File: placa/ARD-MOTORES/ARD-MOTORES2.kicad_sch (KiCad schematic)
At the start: 24 parts, among them J1 Power, J2 Digital/PWM, J3 Analog, J4 Digital/PWM, J5 Conn_01x02, Q1 LFRZ44

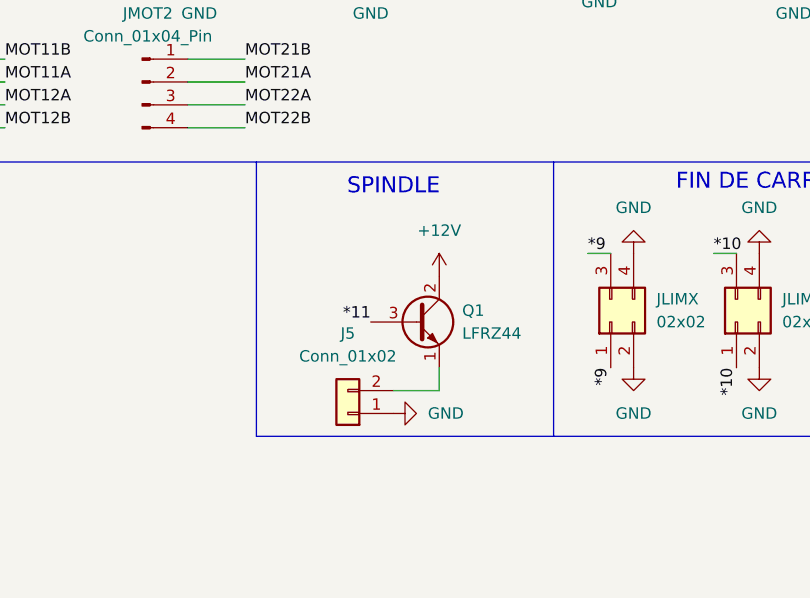
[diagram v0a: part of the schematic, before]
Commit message: arduino como main
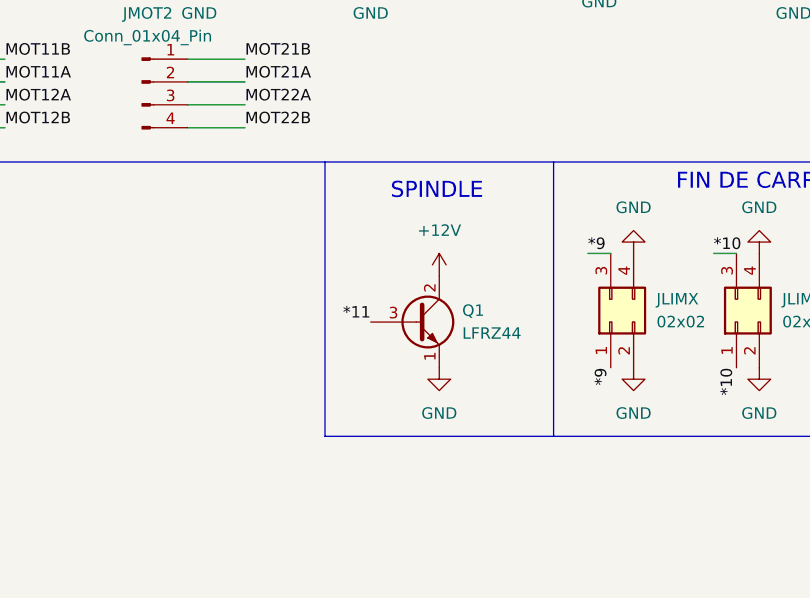
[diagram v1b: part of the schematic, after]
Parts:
- removed J5: Conn_01x02, symbol Connector_Generic:Conn_01x02
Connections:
- net GND: now also Q1.1 (E)
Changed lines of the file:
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@@
 	(polyline
 		(pts
-			(xy 204.47 115.57) (xy 204.47 85.09)
+			(xy 212.09 115.57) (xy 212.09 85.09)
 		)
 		(stroke
@@
 	(polyline
 		(pts
-			(xy 237.49 115.57) (xy 204.47 115.57)
+			(xy 237.49 115.57) (xy 212.09 115.57)
 		)
 		(stroke
@@
 	(wire
 		(pts
-			(xy 224.79 110.49) (xy 224.79 107.95)
-		)
-		(stroke
-			(width 0)
-			(type default)
-		)
-	)
-	(wire
-		(pts
 			(xy 135.89 43.18) (xy 139.7 43.18)
 		)
@@
 	(wire
 		(pts
-			(xy 219.71 110.49) (xy 224.79 110.49)
-		)
-		(stroke
-			(width 0)
-			(type default)
-		)
-	)
-	(wire
-		(pts
 			(xy 62.23 74.93) (xy 74.93 74.93)
 		)
@@
 	(text "SPINDLE"
 		(exclude_from_sim no)
-		(at 219.71 87.884 0)
+		(at 224.536 88.392 0)
 		(effects
 			(font
@@
 	)
 	(symbol
-		(lib_name "GND_1")
+		(lib_name "GND_3")
 		(lib_id "power:GND")
-		(at 219.71 113.03 90)
+		(at 224.79 107.95 0)
 		(unit 1)
 		(exclude_from_sim no)
@@
 		(fields_autoplaced yes)
 		(property "Reference" "#PWR035"
-			(at 226.06 113.03 0)
+			(at 224.79 114.3 0)
 			(effects
 				(font
@@
 		)
 		(property "Value" "GND"
-			(at 223.52 113.0299 90)
+			(at 224.79 113.03 0)
 			(effects
 				(font
 					(size 1.27 1.27)
 				)
-				(justify right)
 			)
 		)
 		(property "Footprint" ""
-			(at 219.71 113.03 0)
+			(at 224.79 107.95 0)
 			(effects
 				(font
@@
 		)
 		(property "Datasheet" ""
-			(at 219.71 113.03 0)
+			(at 224.79 107.95 0)
 			(effects
 				(font
@@
 		)
 		(property "Description" "Power symbol creates a global label with name \"GND\" , ground"
-			(at 219.71 113.03 0)
+			(at 224.79 107.95 0)
 			(effects
 				(font
@@
 					(unit 1)
 				)
-			)
-		)
-	)
-	(symbol
-		(lib_id "Connector_Generic:Conn_01x02")
-		(at 214.63 113.03 180)
-		(unit 1)
-		(exclude_from_sim no)
-		(in_bom yes)
-		(on_board yes)
-		(dnp no)
-		(fields_autoplaced yes)
-		(property "Reference" "J5"
-			(at 214.63 104.14 0)
-			(effects
-				(font
-					(size 1.27 1.27)
-				)
-			)
-		)
-		(property "Value" "Conn_01x02"
-			(at 214.63 106.68 0)
-			(effects
-				(font
-					(size 1.27 1.27)
-				)
-			)
-		)
-		(property "Footprint" ""
-			(at 214.63 113.03 0)
-			(effects
-				(font
-					(size 1.27 1.27)
-				)
-				(hide yes)
-			)
-		)
-		(property "Datasheet" "~"
-			(at 214.63 113.03 0)
-			(effects
-				(font
-					(size 1.27 1.27)
-				)
-				(hide yes)
-			)
-		)
-		(property "Description" "Generic connector, single row, 01x02, script generated (kicad-library-utils/schlib/autogen/connector/)"
-			(at 214.63 113.03 0)
-			(effects
-				(font
-					(size 1.27 1.27)
-				)
-				(hide yes)
-			)
-		)
-		(pin "1"
-		)
-		(pin "2"
-		)
-		(instances
-			(project ""
-				(path "/e63e39d7-6ac0-4ffd-8aa3-1841a4541b55"
-					(reference "J5")
-					(unit 1)
-				)

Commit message: m
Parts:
- removed D2, D3: D_Zener, symbol Device:D_Zener
- removed Q1: LFRZ44, Package_TO_SOT_THT:TO-126-3_Vertical, symbol Transistor_BJT:BF457
- removed out: OUT, symbol Connector:Conn_01x04_Pin
- added D4: LED2, LED_THT:LED_D3.0mm, symbol Device:LED
- added J5: Conn_01x02, TerminalBlock_Phoenix:TerminalBlock_Phoenix_MKDS-1,5-2-5.08_1x02_P5.08mm_Horizontal, symbol Connector_Generic:Conn_01x02
- added JOUT1: Conn_01x02, Connector_PinSocket_2.54mm:PinSocket_1x02_P2.54mm_Vertical, symbol Connector_Generic:Conn_01x02
- added Q1: IRLZ44N, Package_TO_SOT_THT:TO-220-3_Vertical, symbol Transistor_FET:IRLZ44N
- added R2: 1800R, Resistor_THT:R_Axial_DIN0309_L9.0mm_D3.2mm_P12.70mm_Horizontal, symbol Device:R
- added R3: 10R, Resistor_THT:R_Axial_DIN0309_L9.0mm_D3.2mm_P12.70mm_Horizontal, symbol Device:R
- added R4: 10k, Resistor_THT:R_Axial_DIN0309_L9.0mm_D3.2mm_P12.70mm_Horizontal, symbol Device:R
- C1, C2, C3: footprint (none) -> Capacitor_THT:CP_Radial_D8.0mm_P3.80mm
- D1: footprint (none) -> LED_THT:LED_D3.0mm
- JFUENTE1: renamed from JFUENTE; footprint (none) -> TerminalBlock:TerminalBlock_Xinya_XY308-2.54-4P_1x04_P2.54mm_Horizontal
- JLIMX1: renamed from JLIMX; footprint (none) -> Connector_PinSocket_2.54mm:PinSocket_2x02_P2.54mm_Vertical
- JLIMY1: renamed from JLIMY; footprint (none) -> Connector_PinSocket_2.54mm:PinSocket_2x02_P2.54mm_Vertical
- JLIMZ1: renamed from JLIMZ; footprint (none) -> Connector_PinSocket_2.54mm:PinSocket_2x02_P2.54mm_Vertical
- JMOT0, JMOT1, JMOT2: footprint (none) -> Connector_PinSocket_2.54mm:PinSocket_1x04_P2.54mm_Vertical
- R1: value R -> 330R; footprint (none) -> Resistor_THT:R_Axial_DIN0309_L9.0mm_D3.2mm_P12.70mm_Horizontal
- renumbered MOTX to MOTX1, MOTY to MOTY1, MOTZ to MOTZ1
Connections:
- net *10: now also MOTY1.16 (DIR); no longer JLIMY1.1 (Pin_1), JLIMY1.3 (Pin_3)
- net *11: now also MOTY1.15 (STEP), R3.1
- net *3: now also MOTZ1.15 (STEP); no longer MOTY1.15 (STEP)
- net *5: no longer MOTX1.16 (DIR)
- net *6: no longer MOTY1.16 (DIR)
- net +12V: now also J5.1 (Pin_1), R2.1
- net +3V3: now also J1.4 (Pin_4)
- net +5V: now also J1.5 (Pin_5)
- net 12: now also MOTX1.15 (STEP); no longer JLIMZ1.1 (Pin_1), JLIMZ1.3 (Pin_3)
- net 13: now also MOTX1.16 (DIR)
- net 2: now also MOTZ1.16 (DIR); no longer MOTX1.15 (STEP)
- net 4: no longer MOTZ1.15 (STEP)
- net 7: now also JLIMZ1.1 (Pin_1), JLIMZ1.3 (Pin_3); no longer MOTZ1.16 (DIR)
- net 8: now also JLIMY1.1 (Pin_1), JLIMY1.3 (Pin_3)
- net GND: now also Q1.3 (S), R4.1
- net RX/0: now also JOUT1.2 (Pin_2)
- net TX/1: now also JOUT1.1 (Pin_1)
- new net: D4.1 (K), J5.2 (Pin_2), Q1.2 (D)
- new net: D4.2 (A), R2.2
- new net: Q1.1 (G), R3.2, R4.2
